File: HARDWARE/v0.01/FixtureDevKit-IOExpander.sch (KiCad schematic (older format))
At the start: 58 parts

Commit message: o boy
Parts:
- removed J? (x3): Conn_01x04, symbol Conn_01x04
- added J?: IOExp_0, symbol Conn_01x04
- added J? (x2): IOExp_1, symbol Conn_01x04
- J?: value Conn_01x04 -> IOExp_0
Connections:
- net GND: now also J?.3 (Pin_3), J?.3 (Pin_3), J?.3 (Pin_3), J?.3 (Pin_3); no longer J?.4 (Pin_4)
- net SCL: now also J?.1 (Pin_1), J?.1 (Pin_1), J?.1 (Pin_1), J?.1 (Pin_1); no longer J?.3 (Pin_3)
- net SDA: now also J?.2 (Pin_2), J?.2 (Pin_2), J?.2 (Pin_2)
- net VCC-3V3: now also J?.4 (Pin_4), J?.4 (Pin_4), J?.4 (Pin_4), J?.4 (Pin_4); no longer J?.1 (Pin_1)
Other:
- moved on the sheet: J?
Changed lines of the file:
@@
 L Conn_01x04 J?
 U 1 1 59EFBDCF
-P 3250 1700
-F 0 "J?" H 3250 1900 50  0000 C CNN
-F 1 "Conn_01x04" H 3250 1400 50  0000 C CNN
-F 2 "" H 3250 1700 50  0001 C CNN
-F 3 "" H 3250 1700 50  0001 C CNN
-	1    3250 1700
+P 3250 2000
+F 0 "J?" H 3250 2200 50  0000 C CNN
+F 1 "IOExp_0" H 3250 1700 50  0000 C CNN
+F 2 "" H 3250 2000 50  0001 C CNN
+F 3 "" H 3250 2000 50  0001 C CNN
+	1    3250 2000
 	0    -1   -1   0
 $EndComp
-Text Label 3150 2000 3    60   ~ 0
+Text Label 3150 2300 3    60   ~ 0
+SCL
+Text Label 3250 2300 3    60   ~ 0
+SDA
+Text Label 3350 2300 3    60   ~ 0
+GND
+Text Label 3450 2300 3    60   ~ 0
 VCC-3V3
-Text Label 3250 2000 3    60   ~ 0
-SDA
-Text Label 3350 2000 3    60   ~ 0
-SCL
-Text Label 3450 2000 3    60   ~ 0
-GND
 Text Label 2600 3450 2    60   ~ 0
 SDA
@@
 	2600 3550 2700 3550
 Wire Wire Line
-	3450 2000 3450 1900
-Wire Wire Line
-	3350 1900 3350 2000
-Wire Wire Line
-	3250 2000 3250 1900
-Wire Wire Line
-	3150 1900 3150 2000
-$Comp
-L Conn_01x04 J?
-U 1 1 59EFCA72
-P 3200 5700
-F 0 "J?" H 3200 5900 50  0000 C CNN
-F 1 "Conn_01x04" H 3200 5400 50  0000 C CNN
-F 2 "" H 3200 5700 50  0001 C CNN
-F 3 "" H 3200 5700 50  0001 C CNN
-	1    3200 5700
-	0    -1   -1   0
-$EndComp
-Text Label 3100 6000 3    60   ~ 0
-VCC-3V3
-Text Label 3200 6000 3    60   ~ 0
-SDA
-Text Label 3300 6000 3    60   ~ 0
-SCL
-Text Label 3400 6000 3    60   ~ 0
-GND
-Wire Wire Line
-	3400 6000 3400 5900
-Wire Wire Line
-	3300 5900 3300 6000
-Wire Wire Line
-	3200 6000 3200 5900
-Wire Wire Line
-	3100 5900 3100 6000
+	3450 2300 3450 2200
+Wire Wire Line
+	3350 2200 3350 2300
+Wire Wire Line
+	3250 2300 3250 2200
+Wire Wire Line
+	3150 2200 3150 2300
 $Comp
 L TCA6426A U?
@@
 	7900 3350 7000 3350
 Connection ~ 7000 3350
-$Comp
-L Conn_01x04 J?
-U 1 1 59EFEA17
-P 8450 1700
-F 0 "J?" H 8450 1900 50  0000 C CNN
-F 1 "Conn_01x04" H 8450 1400 50  0000 C CNN
-F 2 "" H 8450 1700 50  0001 C CNN
-F 3 "" H 8450 1700 50  0001 C CNN
-	1    8450 1700
-	0    -1   -1   0
-$EndComp
-Text Label 8350 2000 3    60   ~ 0
-VCC-3V3
-Text Label 8450 2000 3    60   ~ 0
-SDA
-Text Label 8550 2000 3    60   ~ 0
-SCL
-Text Label 8650 2000 3    60   ~ 0
-GND
 Text Label 7800 3450 2    60   ~ 0
 SDA
@@
 Wire Wire Line
 	7800 3550 7900 3550
-Wire Wire Line
-	8650 2000 8650 1900
-Wire Wire Line
-	8550 1900 8550 2000
-Wire Wire Line
-	8450 2000 8450 1900
-Wire Wire Line
-	8350 1900 8350 2000
-$Comp
-L Conn_01x04 J?
-U 1 1 59EFEA29
-P 8400 5700
-F 0 "J?" H 8400 5900 50  0000 C CNN
-F 1 "Conn_01x04" H 8400 5400 50  0000 C CNN
-F 2 "" H 8400 5700 50  0001 C CNN
-F 3 "" H 8400 5700 50  0001 C CNN
-	1    8400 5700
-	0    -1   -1   0
-$EndComp
-Text Label 8300 6000 3    60   ~ 0
-VCC-3V3
-Text Label 8400 6000 3    60   ~ 0
-SDA
-Text Label 8500 6000 3    60   ~ 0
-SCL
-Text Label 8600 6000 3    60   ~ 0
-GND
-Wire Wire Line
-	8600 6000 8600 5900
-Wire Wire Line
-	8500 5900 8500 6000
-Wire Wire Line
-	8400 6000 8400 5900
-Wire Wire Line
-	8300 5900 8300 6000
 Text Notes 750  850  0    157  ~ 0
 IO Expander
@@
 Text Notes 8900 5500 0    61   ~ 0
 I2C Addr: 0x23\n
+$Comp
+L Conn_01x04 J?
+U 1 1 59EFECEB
+P 3250 6150
+F 0 "J?" H 3250 6350 50  0000 C CNN
+F 1 "IOExp_0" H 3250 5850 50  0000 C CNN
+F 2 "" H 3250 6150 50  0001 C CNN
+F 3 "" H 3250 6150 50  0001 C CNN
+	1    3250 6150
+	0    -1   1    0
+$EndComp
+Text Label 3150 5850 1    60   ~ 0
+SCL
+Text Label 3250 5850 1    60   ~ 0
+SDA
+Text Label 3350 5850 1    60   ~ 0
+GND
+Text Label 3450 5850 1    60   ~ 0
+VCC-3V3
+Wire Wire Line
+	3450 5850 3450 5950
+Wire Wire Line
+	3350 5950 3350 5850
+Wire Wire Line
+	3250 5850 3250 5950
+Wire Wire Line
+	3150 5950 3150 5850
+$Comp
+L Conn_01x04 J?
+U 1 1 59EFFD29
+P 8450 2000
+F 0 "J?" H 8450 2200 50  0000 C CNN
+F 1 "IOExp_1" H 8450 1700 50  0000 C CNN
+F 2 "" H 8450 2000 50  0001 C CNN
+F 3 "" H 8450 2000 50  0001 C CNN
+	1    8450 2000
+	0    -1   -1   0
+$EndComp
+Text Label 8350 2300 3    60   ~ 0
+SCL
+Text Label 8450 2300 3    60   ~ 0
+SDA
+Text Label 8550 2300 3    60   ~ 0
+GND
+Text Label 8650 2300 3    60   ~ 0
+VCC-3V3
+Wire Wire Line
+	8650 2300 8650 2200
+Wire Wire Line
+	8550 2200 8550 2300
+Wire Wire Line
+	8450 2300 8450 2200
+Wire Wire Line
+	8350 2200 8350 2300
+$Comp
+L Conn_01x04 J?
+U 1 1 59EFFE87
+P 8450 6100
+F 0 "J?" H 8450 6300 50  0000 C CNN
+F 1 "IOExp_1" H 8450 5800 50  0000 C CNN
+F 2 "" H 8450 6100 50  0001 C CNN
+F 3 "" H 8450 6100 50  0001 C CNN
+	1    8450 6100
+	0    -1   1    0
+$EndComp
+Text Label 8350 5800 1    60   ~ 0
+SCL
+Text Label 8450 5800 1    60   ~ 0
+SDA
+Text Label 8550 5800 1    60   ~ 0
+GND
+Text Label 8650 5800 1    60   ~ 0
+VCC-3V3
+Wire Wire Line
+	8650 5800 8650 5900
+Wire Wire Line
+	8550 5900 8550 5800
+Wire Wire Line
+	8450 5800 8450 5900
+Wire Wire Line
+	8350 5900 8350 5800
 $EndSCHEMATC

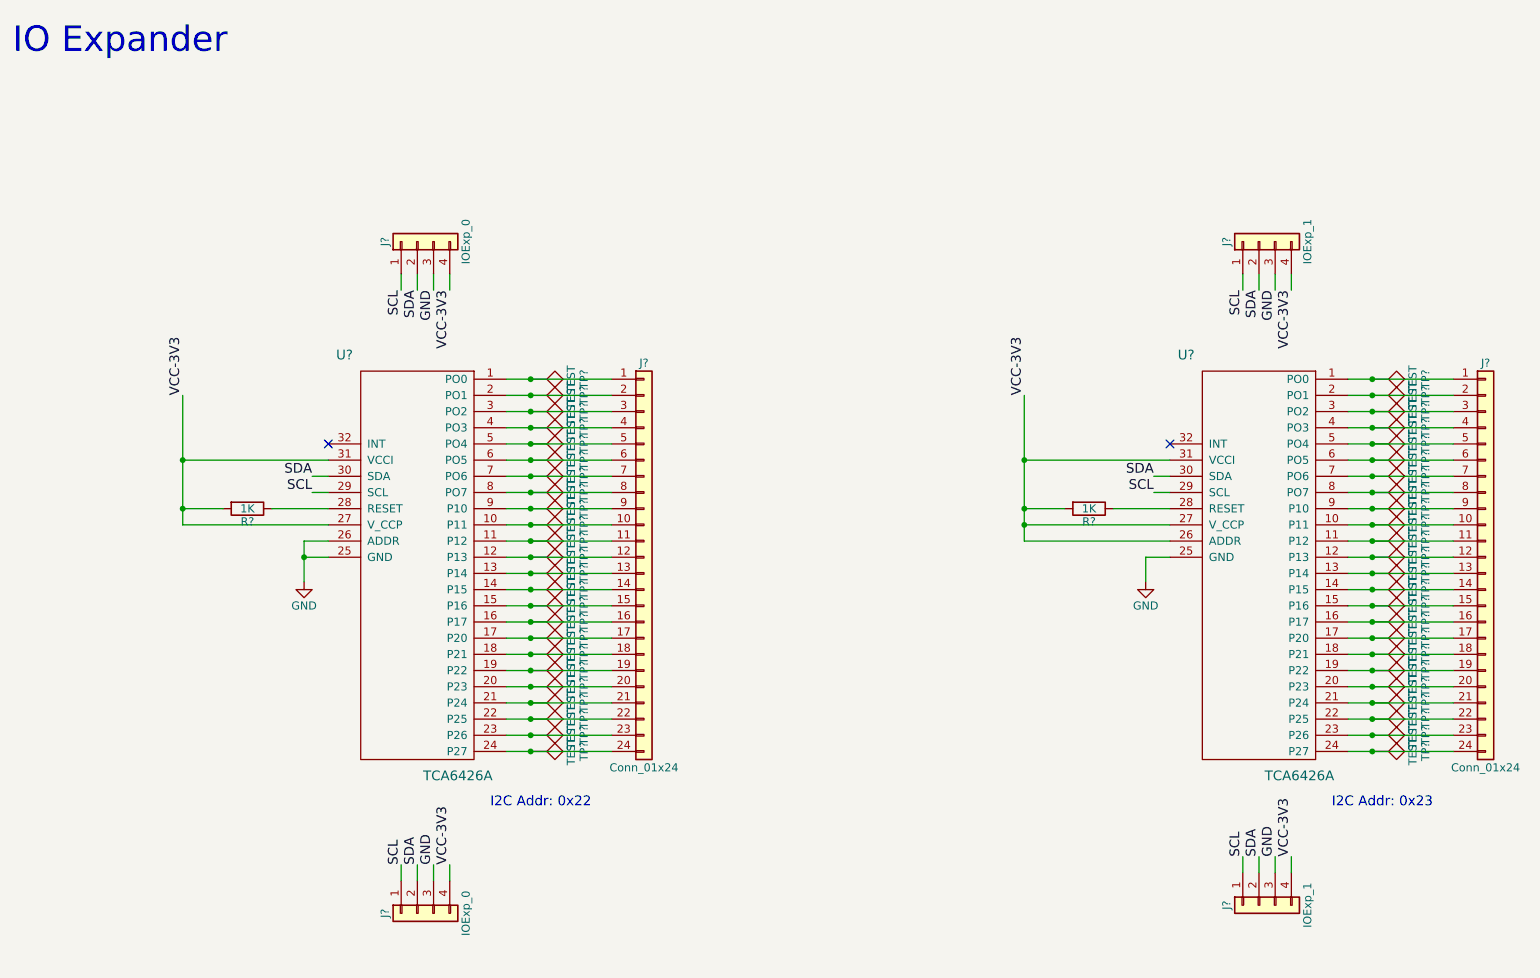
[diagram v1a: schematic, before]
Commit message: adding netlist and design rules check
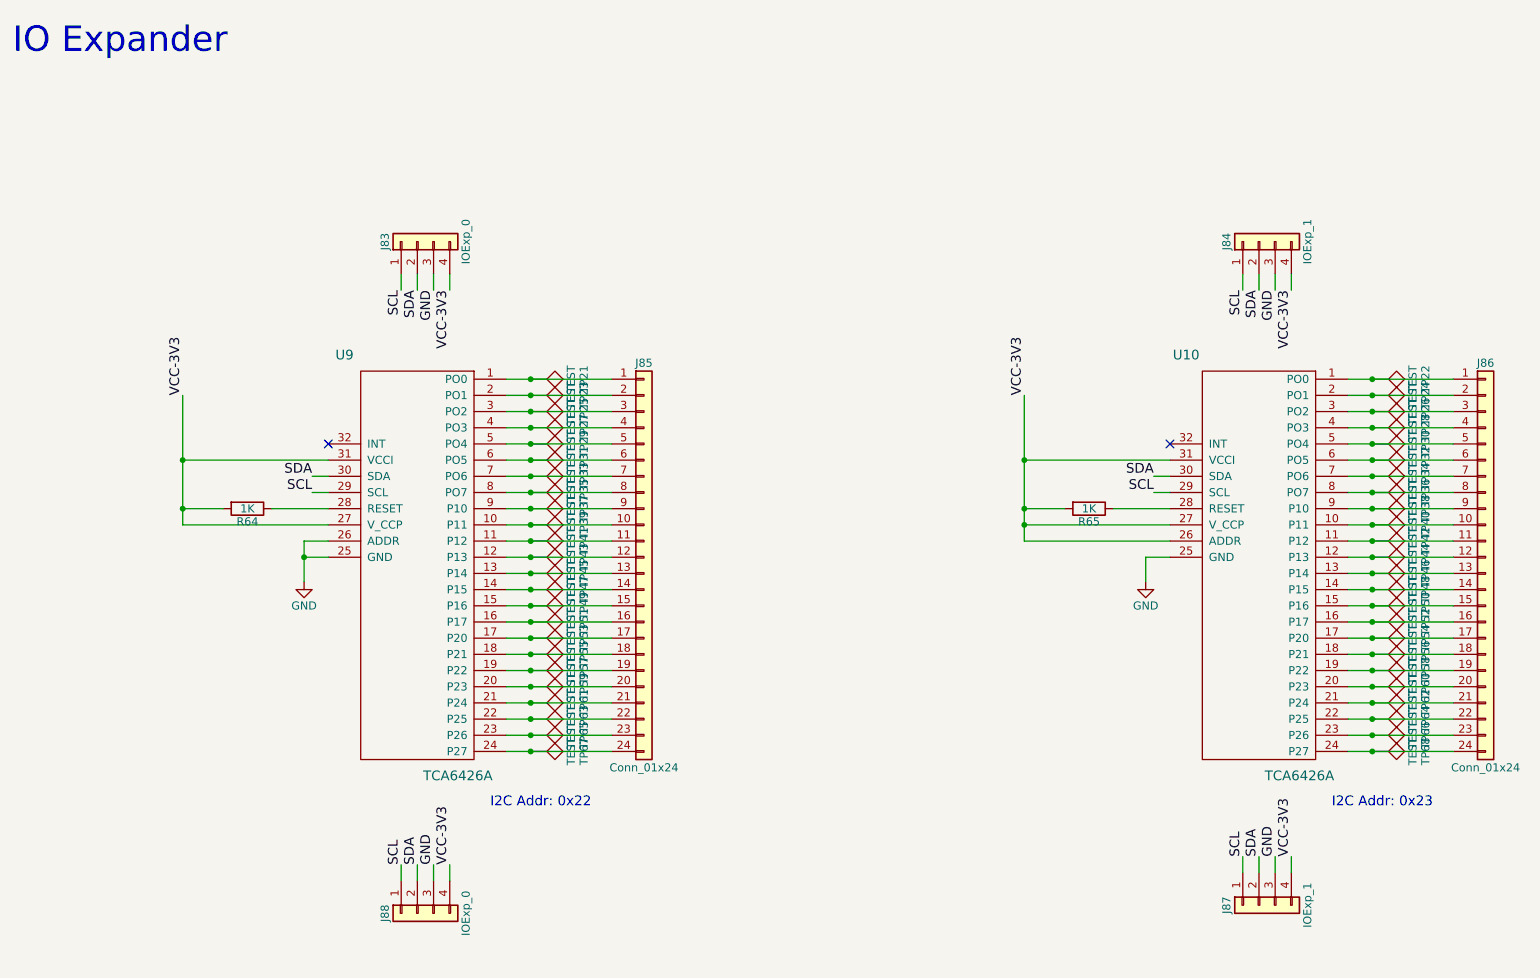
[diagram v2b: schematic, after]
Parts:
- gave numbers to parts that had none: 58
